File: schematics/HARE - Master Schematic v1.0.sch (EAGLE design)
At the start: 93 parts, among them IC1 NE5532N, IC2 NE5532N, IC3 FT232RL, IC4 NE5532N, IC5 7805DT, IC6 AT25P, J1 9V, J2 STEREOSW, J3 STEREOSW, Q1 16 MHz, SW1 3PDT, SW2 Reset Button, U1 ATMEGA328P-PU, U2 MCP4921-E/P, X2 USB-B-H

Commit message: Updated master schematic
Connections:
- net GND: now also IC1P.V-
- net VCC: now also IC1P.V+
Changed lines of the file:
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@@
 <part name="SUPPLY9" library="supply2" deviceset="GND" device=""/>
 <part name="C5" library="resistor" deviceset="C-EU" device="C0805K" value="1uF"/>
+<part name="SUPPLY10" library="supply2" deviceset="GND" device=""/>
+<part name="P+5" library="supply1" deviceset="VCC" device=""/>
 </parts>
 <sheets>
@@
 <instance part="SUPPLY9" gate="GND" x="203.2" y="208.28"/>
 <instance part="C5" gate="G$1" x="139.7" y="215.9" rot="R90"/>
+<instance part="IC1" gate="P" x="309.88" y="233.68"/>
+<instance part="SUPPLY10" gate="GND" x="309.88" y="220.98"/>
+<instance part="P+5" gate="VCC" x="309.88" y="246.38"/>
 </instances>
 <busses>
@@
 <pinref part="P+8" gate="VCC" pin="VCC"/>
 <wire x1="154.94" y1="271.78" x2="154.94" y2="274.32" width="0.1524" layer="91"/>
+</segment>
+<segment>
+<pinref part="IC1" gate="P" pin="V+"/>
+<pinref part="P+5" gate="VCC" pin="VCC"/>
+<wire x1="309.88" y1="241.3" x2="309.88" y2="243.84" width="0.1524" layer="91"/>
 </segment>
 </net>
@@
 <junction x="203.2" y="215.9"/>
 </segment>
+<segment>
+<pinref part="SUPPLY10" gate="GND" pin="GND"/>
+<pinref part="IC1" gate="P" pin="V-"/>
+<wire x1="309.88" y1="223.52" x2="309.88" y2="226.06" width="0.1524" layer="91"/>
+</segment>
 </net>
 <net name="INPUT" class="0">
@@
 </sheet>
 </sheets>
-<errors>
-</errors>
 </schematic>
 </drawing>

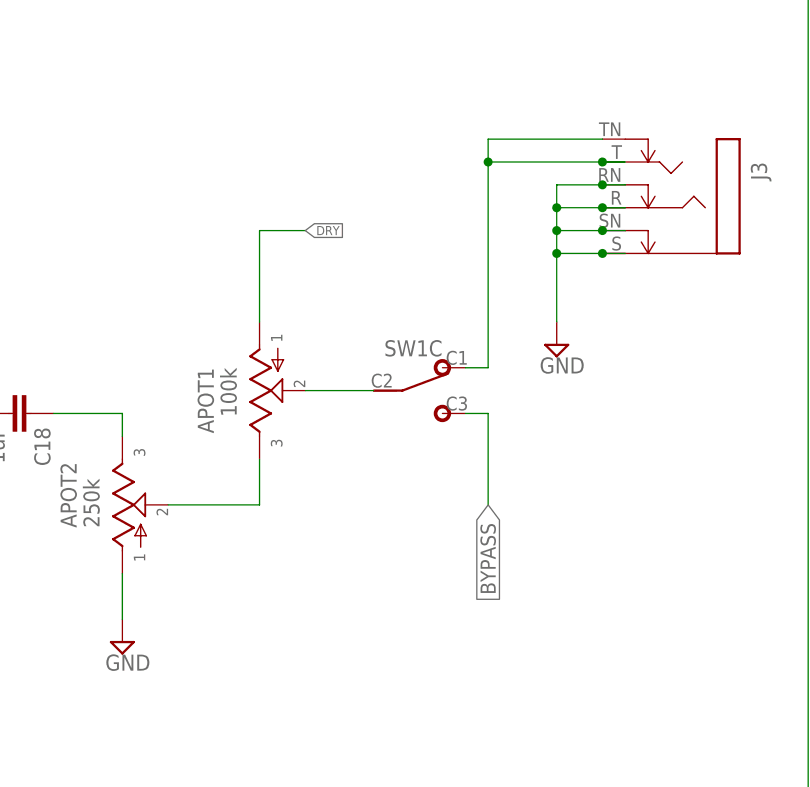
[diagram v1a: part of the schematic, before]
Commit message: Started the eagle layout and fixed a few errors in the schematic
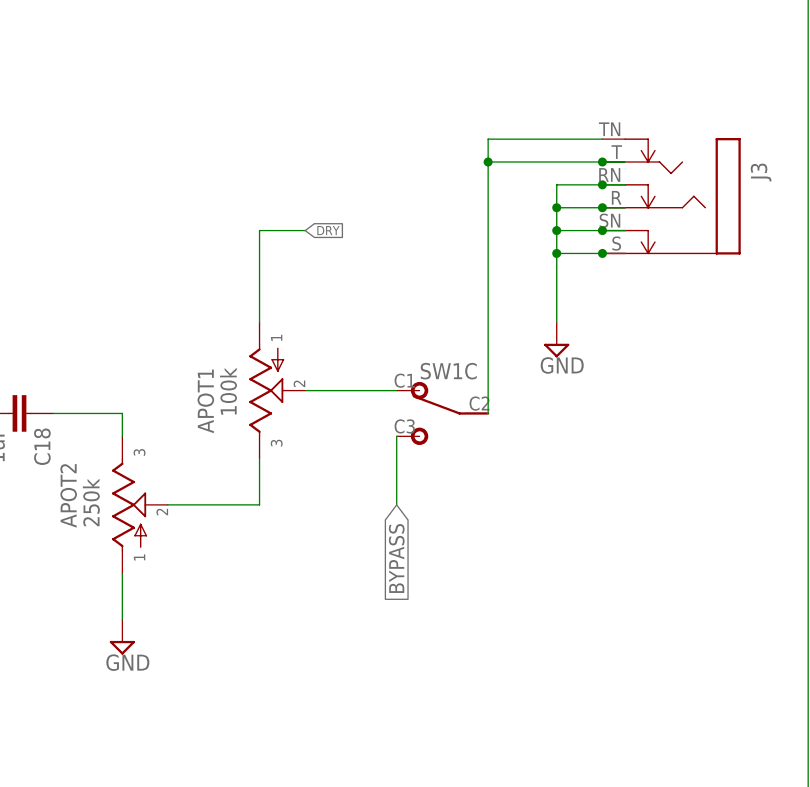
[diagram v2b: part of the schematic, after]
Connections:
- removed net N$47: APOT1.2, SW1C.2
- new net N$15: APOT1.2, SW1C.1
- net N$19: now also SW1C.2; no longer SW1C.1
- net N$36: now also C2.2
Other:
- moved on the sheet: SW1C

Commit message: First pass at board layout and updated schematic
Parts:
- removed C13, C16, C9: 1uF, resistor:C-EUC0805K
- removed C27: 4.7nF, resistor:C-EUC0805K
- removed R29: 1MEG, resistor:R-US_R0805
- removed R34: 3.9k, resistor:R-US_R0805
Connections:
- removed net DAC_OUT: C27.2, R29.1, R34.1
- removed net N$18: C6.1, C9.2, IC1B.OUT, R12.2
- removed net N$23: C13.2, IC2A.OUT, LDR2.2, R14.2, R15.2
- removed net N$34: C16.2, IC2B.OUT, R20.2
- removed net N$50: R29.2, U1.PB2
- removed net N$55: R34.2, U1.PB1
- net EXT_MEM_CS: now also U1.PD4, U2.~CS
- net EXT_MEM_HOLD: now also U1.PD7
- net EXT_MEM_MISO: now also U1.PB4
- net EXT_MEM_MOSI: now also U1.PB5, U2.SDI
- net EXT_MEM_SCK: now also U1.PB3, U2.SCK
- net GND: no longer C27.1
- net VCA_IN: now also IC2A.OUT, LDR2.2, R14.2, R15.2; no longer C13.1
- net VCA_OUT: now also IC2B.OUT, R20.2; no longer C16.1
- net VCF_IN: now also C6.1, IC1B.OUT, R12.2; no longer C9.1

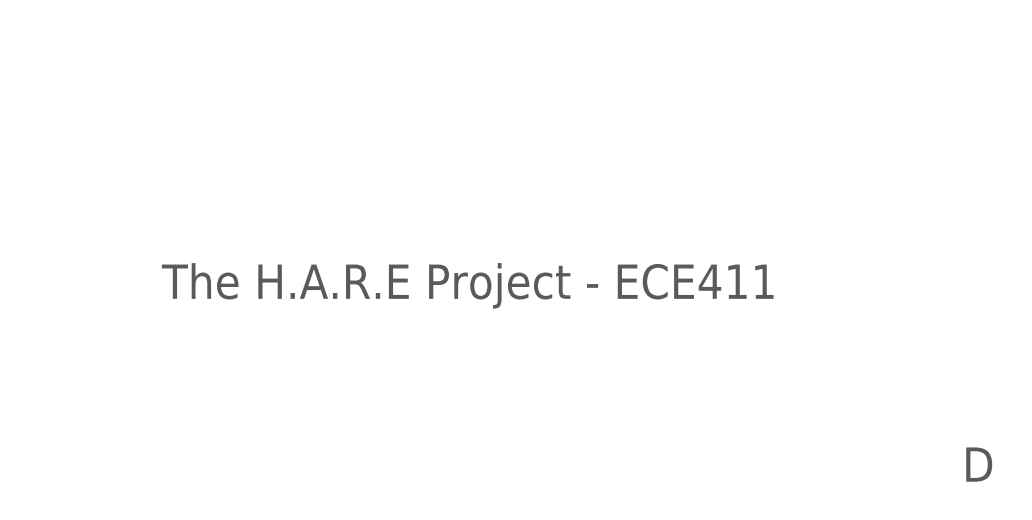
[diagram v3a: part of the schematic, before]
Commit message: Added team number to master schematic
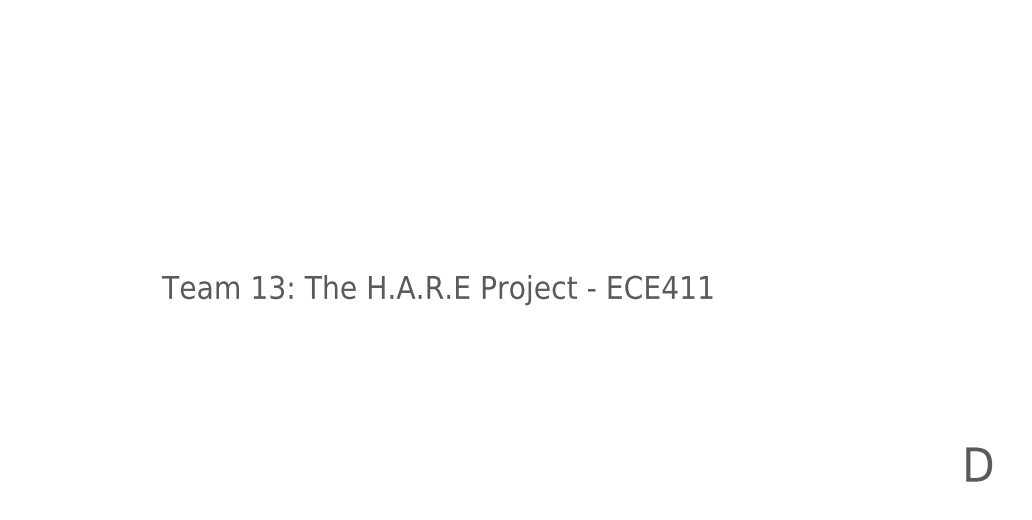
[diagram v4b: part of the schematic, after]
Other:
- note added: "Team 13: The H.A.R.E Project - ECE411"
- note removed: "The H.A.R.E Project - ECE411"
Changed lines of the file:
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@@
 <?xml version="1.0" encoding="utf-8"?>
 <!DOCTYPE eagle SYSTEM "eagle.dtd">
-<eagle version="8.3.1">
+<eagle version="8.4.0">
 <drawing>
 <settings>
@@
 <text x="185.42" y="276.86" size="3.81" layer="97" font="vector" ratio="12">PWMDAC Filter</text>
 <text x="271.78" y="297.18" size="3.81" layer="97" font="vector" ratio="12">External SPI SRAM Memory</text>
-<text x="462.28" y="33.02" size="3.81" layer="97" ratio="14">The H.A.R.E Project - ECE411</text>
+<text x="462.28" y="33.02" size="2.54" layer="97" ratio="14">Team 13: The H.A.R.E Project - ECE411</text>
 <text x="551.18" y="12.7" size="3.81" layer="97" font="vector" ratio="15">D</text>
 </plain>

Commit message: Zack DiD it!
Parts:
- removed C24: 0.1uF, resistor:C-EUC0805K
- removed C30: 10uF, resistor:C-EUC0805K
- added C8: 100nF, resistor:C-EUC0805K
- added R29, R7, R8, R9: 10k, adafruit:R-US_R0805
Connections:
- net EXT_MEM_MISO renamed SPI_MISO
- net EXT_MEM_MOSI renamed SPI_MOSI
- net EXT_MEM_SCK renamed SPI_SCK
- removed net EXT_MEM_CS: IC6.CS/, U1.PD4, U2.~CS
- removed net EXT_MEM_HOLD: IC6.HOLD/, U1.PD7
- removed net N$54: C24.2, IC3.3V3OUT
- new net DAC_CS: R29.1, U1.PD7, U2.~CS
- new net MEM_CS: IC6.CS/, R8.1, U1.PD4
- new net N$34: R7.2
- net 5V: now also C8.2, IC6.HOLD/, R29.2, R7.1, R8.2, R9.1, R9.2; no longer C30.2
- net GND: now also C8.1, IC3.3V3OUT; no longer C24.1, C30.1
- net N$28: now also IC3.OSCO
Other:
- note added: "The H.A.R.E Project - ECE411"
- note removed: "Team 13: The H.A.R.E Project - ECE411"

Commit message: Added IC bypass caps
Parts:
- added C13, C16, C24, C27, C9: .1uF, resistor:C-EUC0805K
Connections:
- net 5V: now also C9.1
- net GND: now also C13.1, C16.2, C24.1, C27.1, C9.2
- net VCC: now also C13.2, C16.1, C24.2, C27.2
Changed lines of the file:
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@@
 <part name="C8" library="resistor" library_urn="urn:adsk.eagle:library:348" deviceset="C-EU" device="C0805K" package3d_urn="urn:adsk.eagle:package:26201/1" value="100nF"/>
 <part name="SUPPLY34" library="supply2" library_urn="urn:adsk.eagle:library:372" deviceset="GND" device=""/>
+<part name="C9" library="resistor" library_urn="urn:adsk.eagle:library:348" deviceset="C-EU" device="C0805K" package3d_urn="urn:adsk.eagle:package:26201/1" value=".1uF"/>
+<part name="SUPPLY39" library="supply2" deviceset="GND" device=""/>
+<part name="C13" library="resistor" library_urn="urn:adsk.eagle:library:348" deviceset="C-EU" device="C0805K" package3d_urn="urn:adsk.eagle:package:26201/1" value=".1uF"/>
+<part name="SUPPLY40" library="supply2" deviceset="GND" device=""/>
+<part name="C16" library="resistor" library_urn="urn:adsk.eagle:library:348" deviceset="C-EU" device="C0805K" package3d_urn="urn:adsk.eagle:package:26201/1" value=".1uF"/>
+<part name="SUPPLY41" library="supply2" deviceset="GND" device=""/>
+<part name="C24" library="resistor" library_urn="urn:adsk.eagle:library:348" deviceset="C-EU" device="C0805K" package3d_urn="urn:adsk.eagle:package:26201/1" value=".1uF"/>
+<part name="SUPPLY42" library="supply2" deviceset="GND" device=""/>
+<part name="C27" library="resistor" library_urn="urn:adsk.eagle:library:348" deviceset="C-EU" device="C0805K" package3d_urn="urn:adsk.eagle:package:26201/1" value=".1uF"/>
+<part name="SUPPLY43" library="supply2" deviceset="GND" device=""/>
 </parts>
 <sheets>
@@
 </instance>
 <instance part="IC2" gate="P" x="464.82" y="210.82" rot="MR0"/>
-<instance part="P+6" gate="VCC" x="464.82" y="223.52"/>
+<instance part="P+6" gate="VCC" x="464.82" y="226.06"/>
 <instance part="SUPPLY12" gate="GND" x="464.82" y="198.12"/>
 <instance part="C10" gate="G$1" x="411.48" y="213.36" rot="R270"/>
@@
 <instance part="IC1" gate="P" x="309.88" y="233.68"/>
 <instance part="SUPPLY10" gate="GND" x="309.88" y="220.98"/>
-<instance part="P+5" gate="VCC" x="309.88" y="246.38"/>
+<instance part="P+5" gate="VCC" x="309.88" y="251.46"/>
 <instance part="R7" gate="G$1" x="320.04" y="373.38" rot="R90"/>
 <instance part="R8" gate="G$1" x="327.66" y="373.38" rot="R90"/>
@@
 <instance part="C8" gate="G$1" x="175.26" y="358.14" rot="R180"/>
 <instance part="SUPPLY34" gate="GND" x="175.26" y="353.06"/>
+<instance part="C9" gate="G$1" x="208.28" y="254"/>
+<instance part="SUPPLY39" gate="GND" x="208.28" y="243.84"/>
+<instance part="C13" gate="G$1" x="322.58" y="243.84" rot="R180"/>
+<instance part="SUPPLY40" gate="GND" x="322.58" y="228.6"/>
+<instance part="C16" gate="G$1" x="474.98" y="220.98"/>
+<instance part="SUPPLY41" gate="GND" x="474.98" y="205.74"/>
+<instance part="C24" gate="G$1" x="124.46" y="241.3" rot="R180"/>
+<instance part="SUPPLY42" gate="GND" x="124.46" y="228.6"/>
+<instance part="C27" gate="G$1" x="383.54" y="330.2" rot="R180"/>
+<instance part="SUPPLY43" gate="GND" x="383.54" y="320.04"/>
 </instances>
 <busses>
@@
 <pinref part="IC2" gate="P" pin="V+"/>
 <pinref part="P+6" gate="VCC" pin="VCC"/>
-<wire x1="464.82" y1="218.44" x2="464.82" y2="220.98" width="0.1524" layer="91"/>
+<wire x1="464.82" y1="218.44" x2="464.82" y2="223.52" width="0.1524" layer="91"/>
+<wire x1="464.82" y1="223.52" x2="474.98" y2="223.52" width="0.1524" layer="91"/>
+<junction x="464.82" y="223.52"/>
+<pinref part="C16" gate="G$1" pin="1"/>
 </segment>
 <segment>
@@
 <pinref part="P+3" gate="VCC" pin="VCC"/>
 <wire x1="114.3" y1="241.3" x2="114.3" y2="246.38" width="0.1524" layer="91"/>
+<wire x1="114.3" y1="246.38" x2="124.46" y2="246.38" width="0.1524" layer="91"/>
+<junction x="114.3" y="246.38"/>
+<pinref part="C24" gate="G$1" pin="2"/>
 </segment>
 <segment>
@@
 <pinref part="IC5" gate="A1" pin="VI"/>
 <wire x1="383.54" y1="340.36" x2="388.62" y2="340.36" width="0.1524" layer="91"/>
+<wire x1="383.54" y1="340.36" x2="383.54" y2="335.28" width="0.1524" layer="91"/>
+<junction x="383.54" y="340.36"/>
+<pinref part="C27" gate="G$1" pin="2"/>
 </segment>
 <segment>
@@
 <pinref part="IC1" gate="P" pin="V+"/>
 <pinref part="P+5" gate="VCC" pin="VCC"/>
-<wire x1="309.88" y1="241.3" x2="309.88" y2="243.84" width="0.1524" layer="91"/>
+<wire x1="309.88" y1="241.3" x2="309.88" y2="248.92" width="0.1524" layer="91"/>
+<wire x1="309.88" y1="248.92" x2="322.58" y2="248.92" width="0.1524" layer="91"/>
+<junction x="309.88" y="248.92"/>
+<pinref part="C13" gate="G$1" pin="2"/>
 </segment>
 </net>
@@
 <pinref part="SUPPLY34" gate="GND" pin="GND"/>
 </segment>
+<segment>
+<pinref part="C9" gate="G$1" pin="2"/>
+<wire x1="208.28" y1="248.92" x2="208.28" y2="246.38" width="0.1524" layer="91"/>
+<pinref part="SUPPLY39" gate="GND" pin="GND"/>
+</segment>
+<segment>
+<pinref part="C13" gate="G$1" pin="1"/>
+<wire x1="322.58" y1="241.3" x2="322.58" y2="231.14" width="0.1524" layer="91"/>
+<pinref part="SUPPLY40" gate="GND" pin="GND"/>
+</segment>
+<segment>
+<pinref part="C16" gate="G$1" pin="2"/>
+<wire x1="474.98" y1="215.9" x2="474.98" y2="208.28" width="0.1524" layer="91"/>
+<pinref part="SUPPLY41" gate="GND" pin="GND"/>
+</segment>
+<segment>
+<pinref part="C24" gate="G$1" pin="1"/>
+<wire x1="124.46" y1="238.76" x2="124.46" y2="231.14" width="0.1524" layer="91"/>
+<pinref part="SUPPLY42" gate="GND" pin="GND"/>
+</segment>
+<segment>
+<pinref part="C27" gate="G$1" pin="1"/>
+<wire x1="383.54" y1="327.66" x2="383.54" y2="322.58" width="0.1524" layer="91"/>
+<pinref part="SUPPLY43" gate="GND" pin="GND"/>
+</segment>
 </net>
 <net name="INPUT" class="0">
@@
 <wire x1="210.82" y1="231.14" x2="203.2" y2="231.14" width="0.1524" layer="91"/>
 <wire x1="203.2" y1="231.14" x2="203.2" y2="236.22" width="0.1524" layer="91"/>
-<wire x1="203.2" y1="243.84" x2="203.2" y2="236.22" width="0.1524" layer="91"/>
+<wire x1="203.2" y1="259.08" x2="203.2" y2="256.54" width="0.1524" layer="91"/>
 <pinref part="U2" gate="A" pin="VDD"/>
+<wire x1="203.2" y1="256.54" x2="203.2" y2="236.22" width="0.1524" layer="91"/>
 <wire x1="203.2" y1="236.22" x2="210.82" y2="236.22" width="0.1524" layer="91"/>
 <junction x="203.2" y="236.22"/>
-<label x="203.2" y="243.84" size="1.016" layer="95" font="vector" rot="R90" xref="yes"/>
-</segment>
-<segment>
+<label x="203.2" y="259.08" size="1.016" layer="95" font="vector" rot="R90" xref="yes"/>
+<wire x1="203.2" y1="256.54" x2="208.28" y2="256.54" width="0.1524" layer="91"/>
+<junction x="203.2" y="256.54"/>
+<pinref part="C9" gate="G$1" pin="1"/>
+</segment>
+<segment>

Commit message: ZACK DEFINITELY DID ITgit add schematics/HARE\ -\ Master\ Schematic\ v1.0.sch schematics/HARE\ -\ Master\ Schematic\ v1.0.brd !
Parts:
- added C29: 1uF, resistor:C-EUC0805K
- C16, C24, C27: value .1uF -> 0.1uF
- R29: device adafruit:R-US_R0805 -> resistor:R-US_R0805
- R7, R8, R9: device adafruit:R-US_R0805 -> rcl:R-US_M0805
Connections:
- removed net 5V: C19.2, C22.2, C23.2, C26.2, C28.2, C8.2, C9.1, DPOT1.3, DPOT2.3, DPOT3.3, IC3.VCC, IC5.VO, IC6.HOLD/, IC6.VCC, IC6.WP/, LDR1.2, R29.2, R33.1, R7.1, R8.2, R9.1, R9.2, U1.AREF, U1.AVCC, U1.VCC, U2.VDD, U2.VREFA, X2.VBUS
- removed net N$34: R7.2
- new net +5V: C19.2, C22.2, C23.2, C26.2, C27.1, C28.2, C8.2, DPOT1.3, DPOT2.3, DPOT3.3, IC3.VCC, IC5.VO, IC6.VCC, LDR1.2, R29.2, R33.1, R7.1, R8.1, R9.1, U1.AREF, U1.AVCC, U1.VCC, U2.VDD, U2.VREFA, X2.VBUS
- new net N$18: IC6.WP/, R8.2
- new net N$54: C24.2, IC3.3V3OUT
- net DAC_CS: now also IC6.HOLD/, R7.2; no longer R29.1, U2.~CS
- net GND: now also C13.2, C27.2, C29.1, C9.1; no longer C13.1, C27.1, C9.2, IC3.3V3OUT
- net MEM_CS: now also R29.1, R9.2, U2.~CS; no longer R8.1
- net N$28: no longer IC3.OSCO
- net VCC: now also C13.1, C29.2, C9.2; no longer C13.2, C24.2, C27.2
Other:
- moved on the sheet: C13, C16, C24, C27, C9, R7, R8, R9

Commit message: Updated VCF and PWM LEDs filters
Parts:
- added C30, C31, C32: 470nF, resistor:C-EU050-035X075
- C11, C12: value 0.22uF -> 100nF
- R15: value 10k -> 47k
- R17: value 10k -> 100k
- R27: value 1k -> 2.2k
- R28: value 1k -> 100k
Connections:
- net GND: now also C30.1, C31.1, C32.1
- net N$57: now also C32.2
- net N$59: now also C30.2
- net N$61: now also C31.2
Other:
- moved on the sheet: D3, D4, D5, R7, R8, R9
